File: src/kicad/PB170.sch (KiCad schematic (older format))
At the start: 51 parts, among them J2 USB_B_Micro, Q1 BC817, Q2 BC817, Q3 BC817, Q4 BC817, SW1 SW_MEC_5E, U1 74HC08, U21 74HC08, U22 74HC74

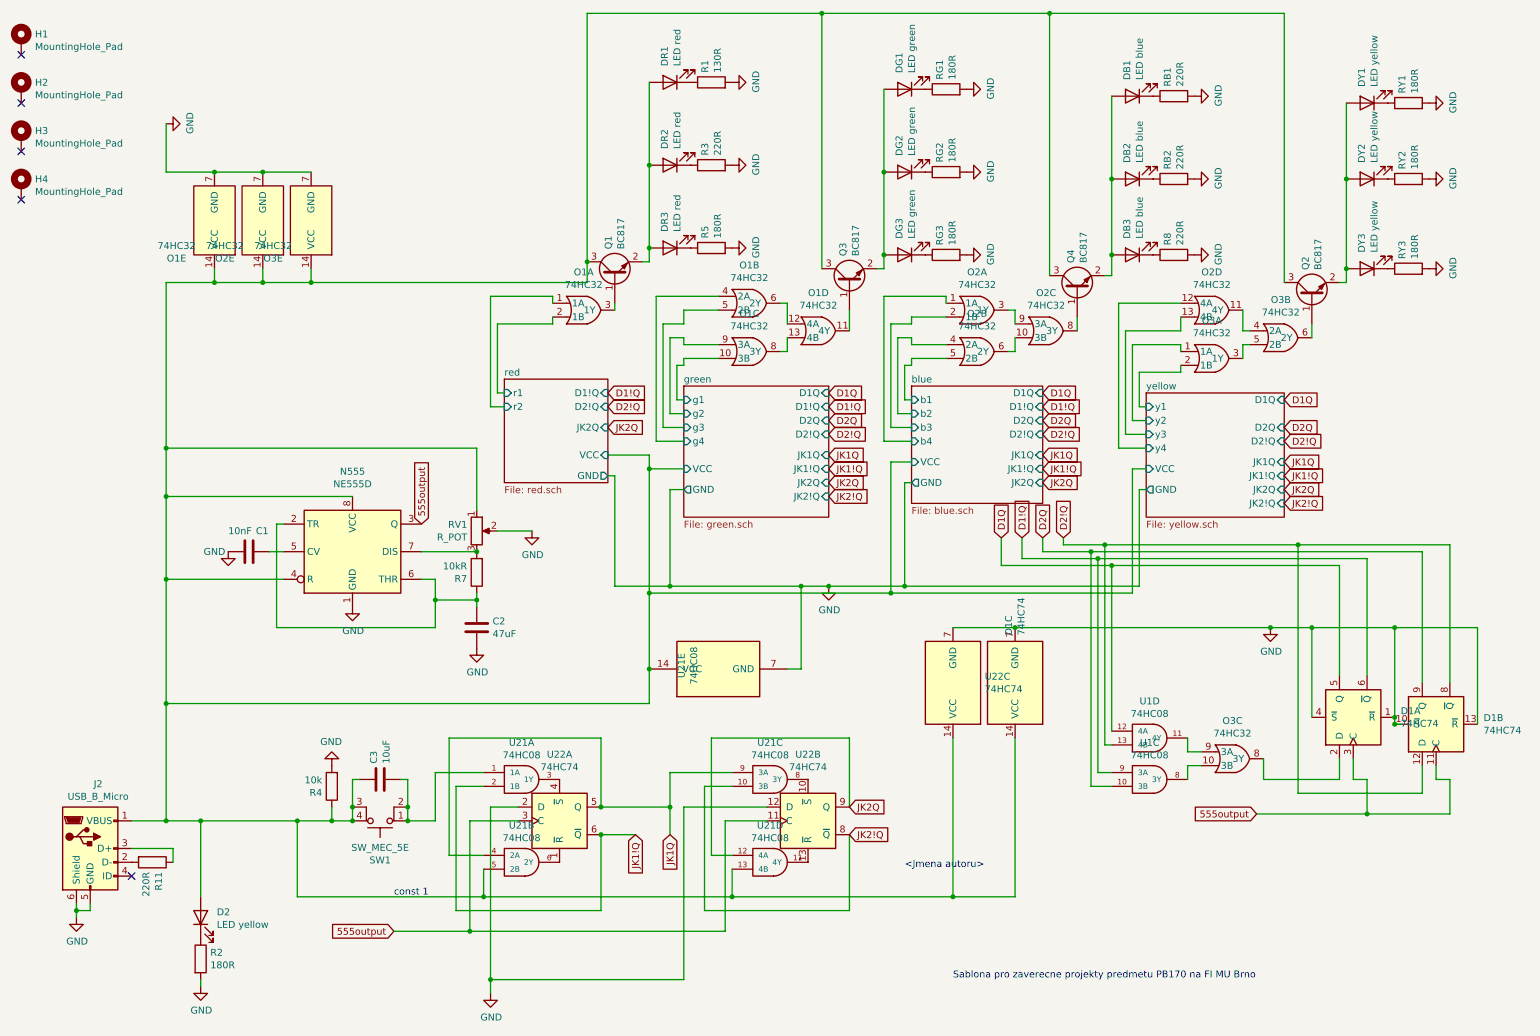
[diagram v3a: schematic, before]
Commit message: Hopefully finished eeschema, added inverters for rs flip flops
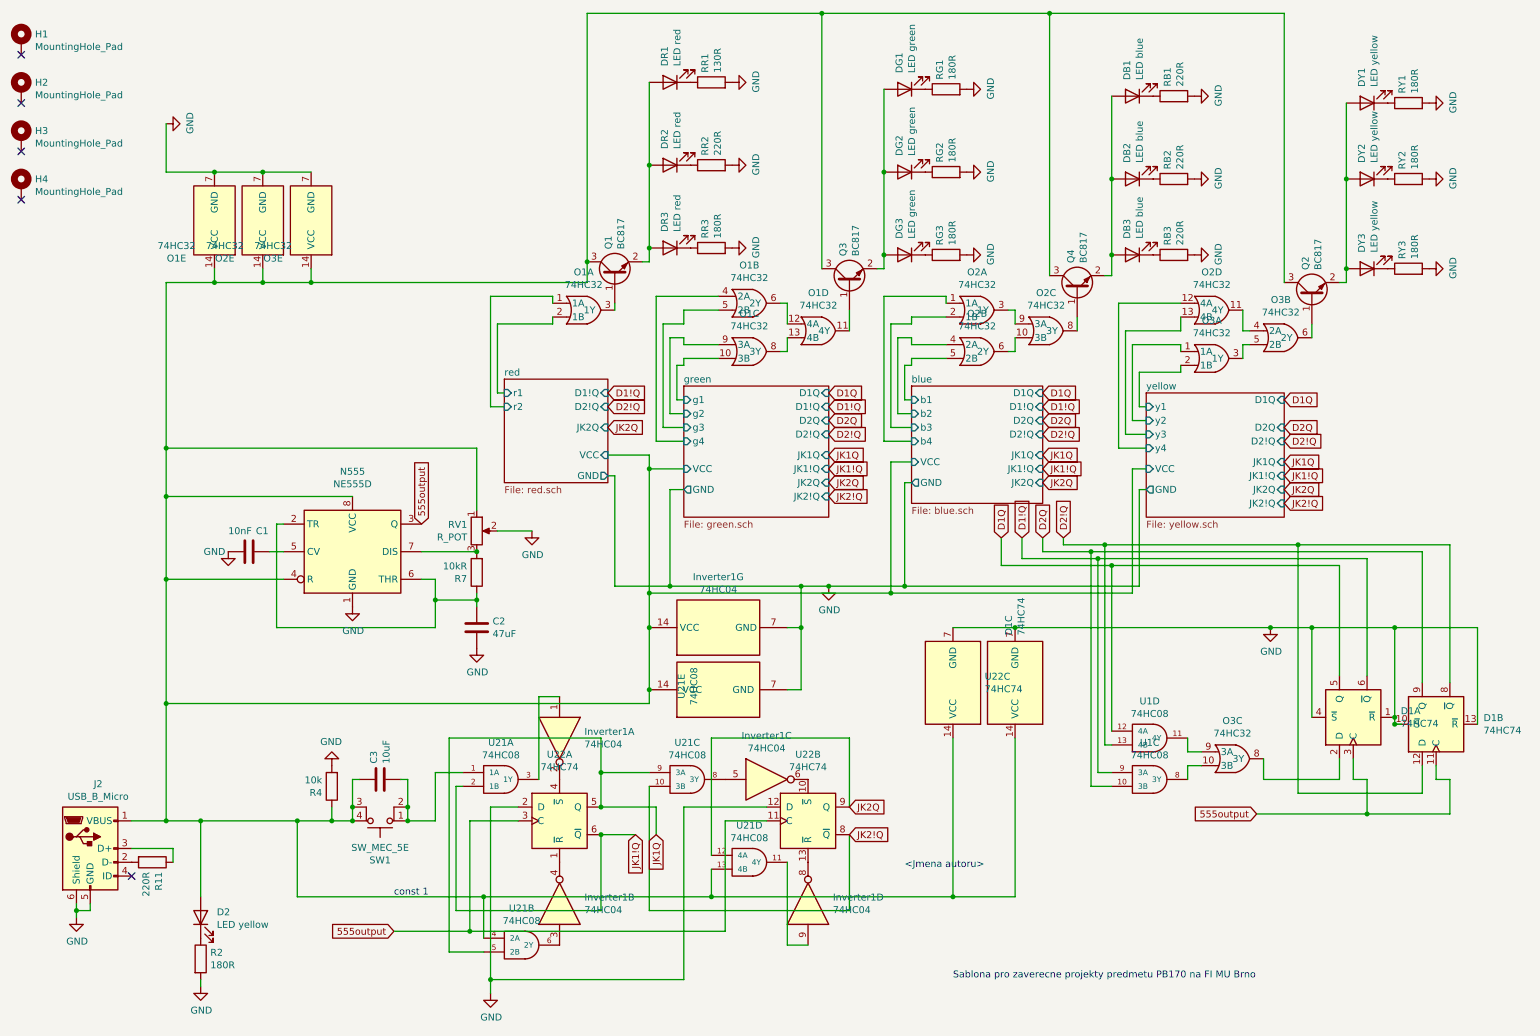
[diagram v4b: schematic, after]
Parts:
- added Inverter1: 74HC04, symbol 74xx:74HC04
- renumbered R8 to RB3, R1 to RR1, R3 to RR2, R5 to RR3
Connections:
- net GND: now also Inverter1.7 (GND)
- net JK1Q: now also U21.5 (2B); no longer U21.4 (2A)
- net blue/VCC: now also U21.4 (2A), Inverter1.14 (VCC); no longer U21.5 (2B)
- net at U22.1 (~R): now also Inverter1.4; no longer U21.6 (2Y)
- net at U22.4 (~S): now also Inverter1.2; no longer U21.3 (1Y)
- net at U21.8 (3Y): now also Inverter1.5; no longer U22.10 (~S)
- net at U21.11 (4Y): now also Inverter1.9; no longer U22.13 (~R)
- new net: Inverter1.1, U21.3 (1Y)
- new net: Inverter1.3, U21.6 (2Y)
- new net: Inverter1.6, U22.10 (~S)
- new net: Inverter1.8, U22.13 (~R)
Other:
- moved on the sheet: U21A, U21B, U21C, U21D, U21E
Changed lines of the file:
@@
 $EndComp
 $Comp
-L Device:R R5
+L Device:R RR3
 U 1 1 5FFFA5F7
 P 5650 2200
-F 0 "R5" H 5720 2246 50  0000 L CNN
+F 0 "RR3" H 5720 2246 50  0000 L CNN
 F 1 "180R" H 5720 2155 50  0000 L CNN
 F 2 "Resistor_SMD:R_0603_1608Metric" V 5580 2200 50  0001 C CNN
@@
 $EndComp
 $Comp
-L Device:R R1
+L Device:R RR1
 U 1 1 5FFFA5FE
 P 5650 1000
-F 0 "R1" H 5720 1046 50  0000 L CNN
+F 0 "RR1" H 5720 1046 50  0000 L CNN
 F 1 "130R" H 5720 955 50  0000 L CNN
 F 2 "Resistor_SMD:R_0603_1608Metric" V 5580 1000 50  0001 C CNN
@@
 $EndComp
 $Comp
-L Device:R R3
+L Device:R RR2
 U 1 1 5FFFA61B
 P 5650 1600
-F 0 "R3" H 5720 1646 50  0000 L CNN
+F 0 "RR2" H 5720 1646 50  0000 L CNN
 F 1 "220R" H 5720 1555 50  0000 L CNN
 F 2 "Resistor_SMD:R_0603_1608Metric" V 5580 1600 50  0001 C CNN
@@
 Wire Wire Line
 	8300 2700 8300 2800
-Text GLabel 5350 6450 3    50   Input ~ 0
+Text GLabel 5250 6450 3    50   Input ~ 0
 JK1Q
 Text GLabel 5100 6450 3    50   Input ~ 0
@@
 $EndComp
 $Comp
-L Device:R R8
+L Device:R RB3
 U 1 1 60201D84
 P 9000 2250
-F 0 "R8" H 9070 2296 50  0000 L CNN
+F 0 "RB3" H 9070 2296 50  0000 L CNN
 F 1 "220R" H 9070 2205 50  0000 L CNN
 F 2 "Resistor_SMD:R_0603_1608Metric" V 8930 2250 50  0001 C CNN
@@
 555output
 Wire Wire Line
-	4850 6250 5350 6250
-Wire Wire Line
-	5350 6250 5350 6450
+	4850 6250 5250 6250
+Wire Wire Line
+	5250 6250 5250 6450
 Wire Wire Line
 	3950 4100 3950 3650
@@
 	6950 4700 8700 4700
 Wire Wire Line
-	5200 5500 5200 5250
+	5200 5500 5200 5400
 Wire Wire Line
 	5200 3800 5450 3800
@@
 L PB170:74HC08 U21
 U 1 1 603E5393
-P 4250 6050
-F 0 "U21" H 4275 6317 50  0000 C CNN
-F 1 "74HC08" H 4275 6226 50  0000 C CNN
-F 2 "Package_SO:SOIC-14_3.9x8.7mm_P1.27mm" H 4250 6050 50  0001 C CNN
-F 3 "https://datasheet.lcsc.com/szlcsc/Nexperia-74HC08D-653_C5593.pdf" H 4250 6050 50  0001 C CNN
-F 4 "C5593" H 4250 6050 50  0001 C CNN "LCSC"
-	1    4250 6050
+P 4100 6050
+F 0 "U21" H 4125 6317 50  0000 C CNN
+F 1 "74HC08" H 4125 6226 50  0000 C CNN
+F 2 "Package_SO:SOIC-14_3.9x8.7mm_P1.27mm" H 4100 6050 50  0001 C CNN
+F 3 "https://datasheet.lcsc.com/szlcsc/Nexperia-74HC08D-653_C5593.pdf" H 4100 6050 50  0001 C CNN
+F 4 "C5593" H 4100 6050 50  0001 C CNN "LCSC"
+	1    4100 6050
 	1    0    0    -1
 $EndComp
@@
 L PB170:74HC08 U21
 U 2 1 603F9FE3
-P 4250 6650
-F 0 "U21" H 4275 6917 50  0000 C CNN
-F 1 "74HC08" H 4275 6826 50  0000 C CNN
-F 2 "Package_SO:SOIC-14_3.9x8.7mm_P1.27mm" H 4250 6650 50  0001 C CNN
-F 3 "https://datasheet.lcsc.com/szlcsc/Nexperia-74HC08D-653_C5593.pdf" H 4250 6650 50  0001 C CNN
-F 4 "C5593" H 4250 6650 50  0001 C CNN "LCSC"
-	2    4250 6650
+P 4250 7250
+F 0 "U21" H 4275 7517 50  0000 C CNN
+F 1 "74HC08" H 4275 7426 50  0000 C CNN
+F 2 "Package_SO:SOIC-14_3.9x8.7mm_P1.27mm" H 4250 7250 50  0001 C CNN
+F 3 "https://datasheet.lcsc.com/szlcsc/Nexperia-74HC08D-653_C5593.pdf" H 4250 7250 50  0001 C CNN
+F 4 "C5593" H 4250 7250 50  0001 C CNN "LCSC"
+	2    4250 7250
 	1    0    0    -1
 $EndComp
@@
 L PB170:74HC08 U21
 U 3 1 6040F23D
-P 6050 6050
-F 0 "U21" H 6075 6317 50  0000 C CNN
-F 1 "74HC08" H 6075 6226 50  0000 C CNN
-F 2 "Package_SO:SOIC-14_3.9x8.7mm_P1.27mm" H 6050 6050 50  0001 C CNN
-F 3 "https://datasheet.lcsc.com/szlcsc/Nexperia-74HC08D-653_C5593.pdf" H 6050 6050 50  0001 C CNN
-F 4 "C5593" H 6050 6050 50  0001 C CNN "LCSC"
-	3    6050 6050
+P 5450 6050
+F 0 "U21" H 5475 6317 50  0000 C CNN
+F 1 "74HC08" H 5475 6226 50  0000 C CNN
+F 2 "Package_SO:SOIC-14_3.9x8.7mm_P1.27mm" H 5450 6050 50  0001 C CNN
+F 3 "https://datasheet.lcsc.com/szlcsc/Nexperia-74HC08D-653_C5593.pdf" H 5450 6050 50  0001 C CNN
+F 4 "C5593" H 5450 6050 50  0001 C CNN "LCSC"
+	3    5450 6050
 	1    0    0    -1
 $EndComp
@@
 L PB170:74HC08 U21
 U 4 1 604215E8
-P 6050 6650
-F 0 "U21" H 6075 6917 50  0000 C CNN
-F 1 "74HC08" H 6075 6826 50  0000 C CNN
-F 2 "Package_SO:SOIC-14_3.9x8.7mm_P1.27mm" H 6050 6650 50  0001 C CNN
-F 3 "https://datasheet.lcsc.com/szlcsc/Nexperia-74HC08D-653_C5593.pdf" H 6050 6650 50  0001 C CNN
-F 4 "C5593" H 6050 6650 50  0001 C CNN "LCSC"
-	4    6050 6650
+P 5900 6650
+F 0 "U21" H 5925 6917 50  0000 C CNN
+F 1 "74HC08" H 5925 6826 50  0000 C CNN
+F 2 "Package_SO:SOIC-14_3.9x8.7mm_P1.27mm" H 5900 6650 50  0001 C CNN
+F 3 "https://datasheet.lcsc.com/szlcsc/Nexperia-74HC08D-653_C5593.pdf" H 5900 6650 50  0001 C CNN
+F 4 "C5593" H 5900 6650 50  0001 C CNN "LCSC"
+	4    5900 6650
 	1    0    0    -1
 $EndComp
@@
 L PB170:74HC08 U21
 U 5 1 604332F0
-P 5700 5250
-F 0 "U21" H 5725 5517 50  0000 C CNN
-F 1 "74HC08" H 5725 5426 50  0000 C CNN
-F 2 "Package_SO:SOIC-14_3.9x8.7mm_P1.27mm" H 5700 5250 50  0001 C CNN
-F 3 "https://datasheet.lcsc.com/szlcsc/Nexperia-74HC08D-653_C5593.pdf" H 5700 5250 50  0001 C CNN
-F 4 "C5593" H 5700 5250 50  0001 C CNN "LCSC"
-	5    5700 5250
-	0    -1   -1   0
-$EndComp
-Connection ~ 5200 5250
-Wire Wire Line
-	5200 5250 5200 4700
-Wire Wire Line
-	6300 5250 6200 5250
-Wire Wire Line
-	6300 5250 6300 4650
+P 5700 5400
+F 0 "U21" H 5725 5667 50  0000 C CNN
+F 1 "74HC08" H 5725 5576 50  0000 C CNN
+F 2 "Package_SO:SOIC-14_3.9x8.7mm_P1.27mm" H 5700 5400 50  0001 C CNN
+F 3 "https://datasheet.lcsc.com/szlcsc/Nexperia-74HC08D-653_C5593.pdf" H 5700 5400 50  0001 C CNN
+F 4 "C5593" H 5700 5400 50  0001 C CNN "LCSC"
+	5    5700 5400
+	0    -1   -1   0
+$EndComp
+Connection ~ 5200 5400
+Wire Wire Line
+	5200 5400 5200 4950
+Wire Wire Line
+	6300 5400 6200 5400
+Wire Wire Line
+	6300 5400 6300 4950
 Connection ~ 6300 4650
 Wire Wire Line
@@
 	5650 5750 5650 6600
 Wire Wire Line
-	5650 6600 5800 6600
-Wire Wire Line
 	6650 6450 6650 7000
-Wire Wire Line
-	6650 7000 5600 7000
-Wire Wire Line
-	5600 7000 5600 6100
-Wire Wire Line
-	5600 6100 5800 6100
-Wire Wire Line
-	5800 6900 5800 6700
-Connection ~ 5800 6900
-Wire Wire Line
-	5350 6250 5350 6000
-Wire Wire Line
-	5350 6000 5800 6000
-Connection ~ 5350 6250
-Wire Wire Line
-	4000 6700 4000 6900
 Connection ~ 4000 6900
-Wire Wire Line
-	4000 6900 5800 6900
-Wire Wire Line
-	4000 6600 3750 6600
-Wire Wire Line
-	3750 6600 3750 5750
 Connection ~ 4850 6250
 Wire Wire Line
@@
 	3800 7000 3800 6100
 Wire Wire Line
-	3800 6100 4000 6100
+	3800 6100 3850 6100
 Connection ~ 4850 6450
 Wire Wire Line
@@
 	3650 6350 3650 6000
 Wire Wire Line
-	3650 6000 4000 6000
+	3650 6000 3850 6000
 Connection ~ 3450 6350
 Wire Wire Line
@@
 	3750 5750 4850 5750
 Wire Wire Line
-	4850 5750 4850 6250
+	4850 5750 4850 6000
 $Comp
 L power:GND #PWR0110
@@
 Wire Wire Line
 	7400 4950 7850 4950
-Wire Wire Line
-	5800 6900 7400 6900
 $Comp
 L 74xx:74HC74 U22
@@
 	-1   0    0    1
 $EndComp
+$Comp
+L 74xx:74HC04 Inverter1
+U 7 1 6030469B
+P 5700 4950
+F 0 "Inverter1" V 6067 4950 50  0000 C CNN
+F 1 "74HC04" V 5976 4950 50  0000 C CNN
+F 2 "" H 5700 4950 50  0001 C CNN
+F 3 "https://assets.nexperia.com/documents/data-sheet/74HC_HCT04.pdf" H 5700 4950 50  0001 C CNN
+	7    5700 4950
+	0    -1   -1   0
+$EndComp
+Connection ~ 5200 4950
+Wire Wire Line
+	5200 4950 5200 4700
+Wire Wire Line
+	6200 4950 6300 4950
+Connection ~ 6300 4950
+Wire Wire Line
+	6300 4950 6300 4650
+$Comp
+L 74xx:74HC04 Inverter1
+U 1 1 60383001
+P 4550 5750
+F 0 "Inverter1" V 4504 5930 50  0000 L CNN
+F 1 "74HC04" V 4595 5930 50  0000 L CNN
+F 2 "" H 4550 5750 50  0001 C CNN
+F 3 "https://assets.nexperia.com/documents/data-sheet/74HC_HCT04.pdf" H 4550 5750 50  0001 C CNN
+F 4 " C5590" V 4550 5750 50  0001 C CNN "LCSC"
+	1    4550 5750
+	0    1    1    0
+$EndComp
+Wire Wire Line
+	4400 6050 4400 5450
+Wire Wire Line
+	4400 5450 4550 5450
+$Comp
+L 74xx:74HC04 Inverter1
+U 2 1 603C8F59
+P 4550 6950
+F 0 "Inverter1" V 4596 6770 50  0000 R CNN
+F 1 "74HC04" V 4505 6770 50  0000 R CNN
+F 2 "" H 4550 6950 50  0001 C CNN
+F 3 "https://assets.nexperia.com/documents/data-sheet/74HC_HCT04.pdf" H 4550 6950 50  0001 C CNN
+F 4 " C5590" V 4550 6950 50  0001 C CNN "LCSC"
+	2    4550 6950
+	0    -1   -1   0
+$EndComp
+Wire Wire Line
+	4000 6900 4000 7200
+Wire Wire Line
+	4000 7300 3750 7300
+Wire Wire Line
+	3750 5750 3750 7300
+$Comp
+L 74xx:74HC04 Inverter1
+U 3 1 6043A8AE
+P 6050 6050
+F 0 "Inverter1" H 6050 6367 50  0000 C CNN
+F 1 "74HC04" H 6050 6276 50  0000 C CNN
+F 2 "" H 6050 6050 50  0001 C CNN
+F 3 "https://assets.nexperia.com/documents/data-sheet/74HC_HCT04.pdf" H 6050 6050 50  0001 C CNN
+F 4 " C5590" V 6050 6050 50  0001 C CNN "LCSC"
+	3    6050 6050
+	1    0    0    -1
+$EndComp
+Wire Wire Line
+	5200 6000 4850 6000
+Connection ~ 4850 6000
+Wire Wire Line
+	4850 6000 4850 6250
+Wire Wire Line
+	5200 6100 5200 7000
+Wire Wire Line
+	5200 7000 6650 7000
+$Comp
+L 74xx:74HC04 Inverter1
+U 4 1 604CB9B5
+P 6350 6950
+F 0 "Inverter1" V 6396 6770 50  0000 R CNN
+F 1 "74HC04" V 6305 6770 50  0000 R CNN
+F 2 "" H 6350 6950 50  0001 C CNN
+F 3 "https://assets.nexperia.com/documents/data-sheet/74HC_HCT04.pdf" H 6350 6950 50  0001 C CNN
+F 4 " C5590" V 6350 6950 50  0001 C CNN "LCSC"
+	4    6350 6950
+	0    -1   -1   0
+$EndComp
+Wire Wire Line
+	4000 6900 5650 6900
+Wire Wire Line
+	6200 6650 6200 7250
+Wire Wire Line
+	6200 7250 6350 7250
+Wire Wire Line
+	5650 6700 5650 6900
+Connection ~ 5650 6900
+Wire Wire Line
+	5650 6900 7400 6900
 $EndSCHEMATC

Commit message: routing finished
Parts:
- Inverter1: footprint (none) -> Package_SO:SOIC-14_3.9x8.7mm_P1.27mm
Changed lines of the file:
@@
 F 0 "Inverter1" V 6067 4950 50  0000 C CNN
 F 1 "74HC04" V 5976 4950 50  0000 C CNN
-F 2 "" H 5700 4950 50  0001 C CNN
+F 2 "Package_SO:SOIC-14_3.9x8.7mm_P1.27mm" H 5700 4950 50  0001 C CNN
 F 3 "https://assets.nexperia.com/documents/data-sheet/74HC_HCT04.pdf" H 5700 4950 50  0001 C CNN
 	7    5700 4950
@@
 F 0 "Inverter1" V 4504 5930 50  0000 L CNN
 F 1 "74HC04" V 4595 5930 50  0000 L CNN
-F 2 "" H 4550 5750 50  0001 C CNN
+F 2 "Package_SO:SOIC-14_3.9x8.7mm_P1.27mm" H 4550 5750 50  0001 C CNN
 F 3 "https://assets.nexperia.com/documents/data-sheet/74HC_HCT04.pdf" H 4550 5750 50  0001 C CNN
 F 4 " C5590" V 4550 5750 50  0001 C CNN "LCSC"
@@
 F 0 "Inverter1" V 4596 6770 50  0000 R CNN
 F 1 "74HC04" V 4505 6770 50  0000 R CNN
-F 2 "" H 4550 6950 50  0001 C CNN
+F 2 "Package_SO:SOIC-14_3.9x8.7mm_P1.27mm" H 4550 6950 50  0001 C CNN
 F 3 "https://assets.nexperia.com/documents/data-sheet/74HC_HCT04.pdf" H 4550 6950 50  0001 C CNN
 F 4 " C5590" V 4550 6950 50  0001 C CNN "LCSC"
@@
 F 0 "Inverter1" H 6050 6367 50  0000 C CNN
 F 1 "74HC04" H 6050 6276 50  0000 C CNN
-F 2 "" H 6050 6050 50  0001 C CNN
+F 2 "Package_SO:SOIC-14_3.9x8.7mm_P1.27mm" H 6050 6050 50  0001 C CNN
 F 3 "https://assets.nexperia.com/documents/data-sheet/74HC_HCT04.pdf" H 6050 6050 50  0001 C CNN
 F 4 " C5590" V 6050 6050 50  0001 C CNN "LCSC"
@@
 F 0 "Inverter1" V 6396 6770 50  0000 R CNN
 F 1 "74HC04" V 6305 6770 50  0000 R CNN
-F 2 "" H 6350 6950 50  0001 C CNN
+F 2 "Package_SO:SOIC-14_3.9x8.7mm_P1.27mm" H 6350 6950 50  0001 C CNN
 F 3 "https://assets.nexperia.com/documents/data-sheet/74HC_HCT04.pdf" H 6350 6950 50  0001 C CNN
 F 4 " C5590" V 6350 6950 50  0001 C CNN "LCSC"

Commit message: resolved push colisions
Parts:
- RR1: value 130R -> 220R; LCSC C22796 -> C22962
- RR3: value 180R -> 220R; LCSC C22828 -> C22962
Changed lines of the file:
@@
 F 1 "USB_B_Micro" H 1207 6926 50  0000 C CNN
 F 2 "PB170:MICRO-USB-SMD_MICROXNJ" H 1300 6500 50  0001 C CNN
-F 3 "~" H 1300 6500 50  0001 C CNN
+F 3 "https://datasheet.lcsc.com/szlcsc/1912111437_SHOU-HAN-MicroXNJ_C404969.pdf" H 1300 6500 50  0001 C CNN
 F 4 "C404969" H 1150 6550 50  0001 C CNN "LCSC"
 	1    1150 6550
@@
 	1    5350 1000
 	-1   0    0    1
-$EndComp
-$Comp
-L Device:R RR3
-U 1 1 5FFFA5F7
-P 5650 2200
-F 0 "RR3" H 5720 2246 50  0000 L CNN
-F 1 "180R" H 5720 2155 50  0000 L CNN
-F 2 "Resistor_SMD:R_0603_1608Metric" V 5580 2200 50  0001 C CNN
-F 3 "https://datasheet.lcsc.com/szlcsc/Uniroyal-Elec-0603WAF1800T5E_C22828.pdf" H 5650 2200 50  0001 C CNN
-F 4 "C22828" H 5650 2200 50  0001 C CNN "LCSC"
-	1    5650 2200
-	0    -1   -1   0
-$EndComp
-$Comp
-L Device:R RR1
-U 1 1 5FFFA5FE
-P 5650 1000
-F 0 "RR1" H 5720 1046 50  0000 L CNN
-F 1 "130R" H 5720 955 50  0000 L CNN
-F 2 "Resistor_SMD:R_0603_1608Metric" V 5580 1000 50  0001 C CNN
-F 3 "https://datasheet.lcsc.com/szlcsc/Uniroyal-Elec-0603WAF1300T5E_C22796.pdf" H 5650 1000 50  0001 C CNN
-F 4 "C22796" H 5650 1000 50  0001 C CNN "LCSC"
-	1    5650 1000
-	0    -1   -1   0
 $EndComp
 $Comp
@@
 Wire Wire Line
 	5650 6900 7400 6900
+$Comp
+L Device:R RR3
+U 1 1 6031EE60
+P 5650 2200
+F 0 "RR3" H 5720 2246 50  0000 L CNN
+F 1 "220R" H 5720 2155 50  0000 L CNN
+F 2 "Resistor_SMD:R_0603_1608Metric" V 5580 2200 50  0001 C CNN
+F 3 "https://datasheet.lcsc.com/szlcsc/Uniroyal-Elec-0603WAF2200T5E_C22962.pdf" H 5650 2200 50  0001 C CNN
+F 4 "C22962" H 5650 2200 50  0001 C CNN "LCSC"
+	1    5650 2200
+	0    -1   -1   0
+$EndComp
+$Comp
+L Device:R RR1
+U 1 1 6033A116
+P 5650 1000
+F 0 "RR1" H 5720 1046 50  0000 L CNN
+F 1 "220R" H 5720 955 50  0000 L CNN
+F 2 "Resistor_SMD:R_0603_1608Metric" V 5580 1000 50  0001 C CNN
+F 3 "https://datasheet.lcsc.com/szlcsc/Uniroyal-Elec-0603WAF2200T5E_C22962.pdf" H 5650 1000 50  0001 C CNN
+F 4 "C22962" H 5650 1000 50  0001 C CNN "LCSC"
+	1    5650 1000
+	0    -1   -1   0
+$EndComp
 $EndSCHEMATC
